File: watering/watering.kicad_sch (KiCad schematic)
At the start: 20 parts, among them J1 Screw_Terminal_01x02, J2 Screw_Terminal_01x03, J3 Screw_Terminal_01x02, J4 Screw_Terminal_01x02, J5 Screw_Terminal_01x03, J6 Screw_Terminal_01x02, J7 Screw_Terminal_01x02

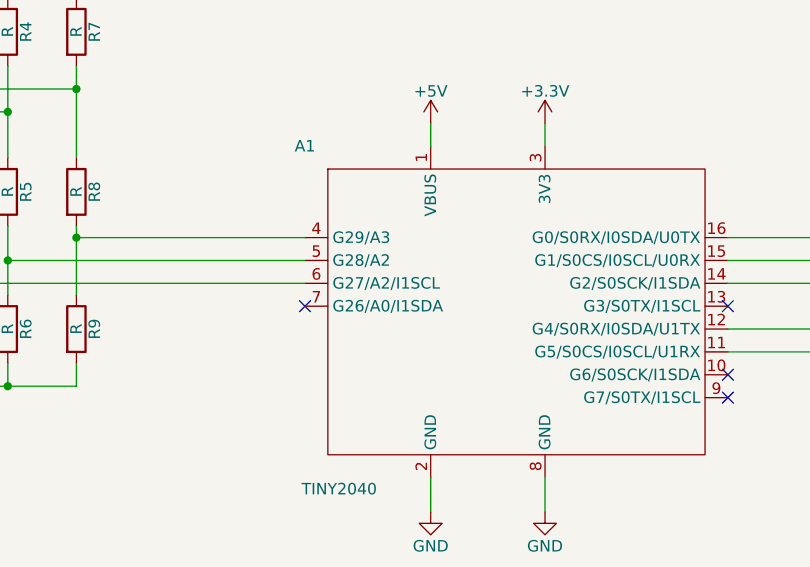
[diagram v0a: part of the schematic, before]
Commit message: Update the tiny2040 symbol.
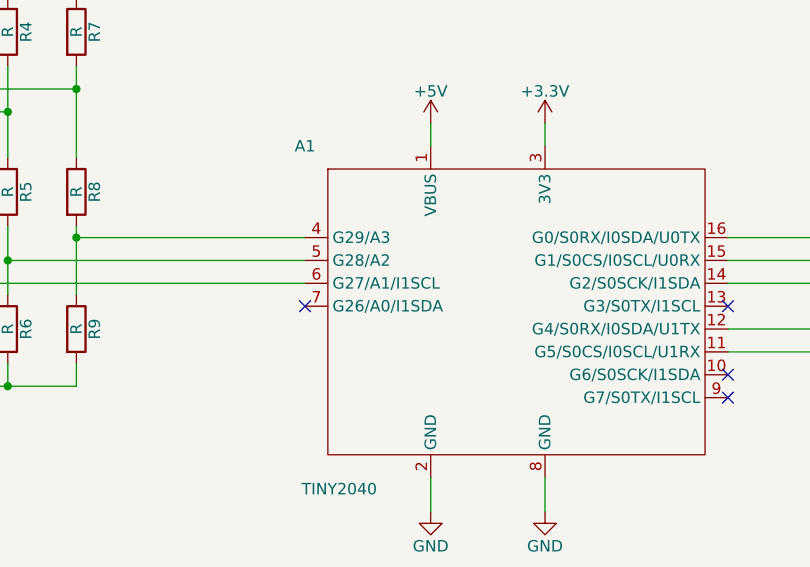
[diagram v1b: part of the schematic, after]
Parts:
- A1: footprint watering:TINY2040 -> watering:Tiny2040
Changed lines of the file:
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@@
       (effects (font (size 1.27 1.27)))
     )
-    (property "Footprint" "watering:TINY2040" (at 99.06 69.85 0)
+    (property "Footprint" "watering:Tiny2040" (at 99.06 69.85 0)
       (effects (font (size 1.27 1.27)) hide)
     )
